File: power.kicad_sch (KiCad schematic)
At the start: 34 parts, among them J11 CON-SOCJ-2155, J12 Header for power lead to QMTE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, J15 Fuse Holder 5A, J33 Header for power lead to QMTE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, J34 Conn_01x04, J35 Conn_01x04, SW2 SW_SPDT_with_shield, U15 LM2678T-5.0

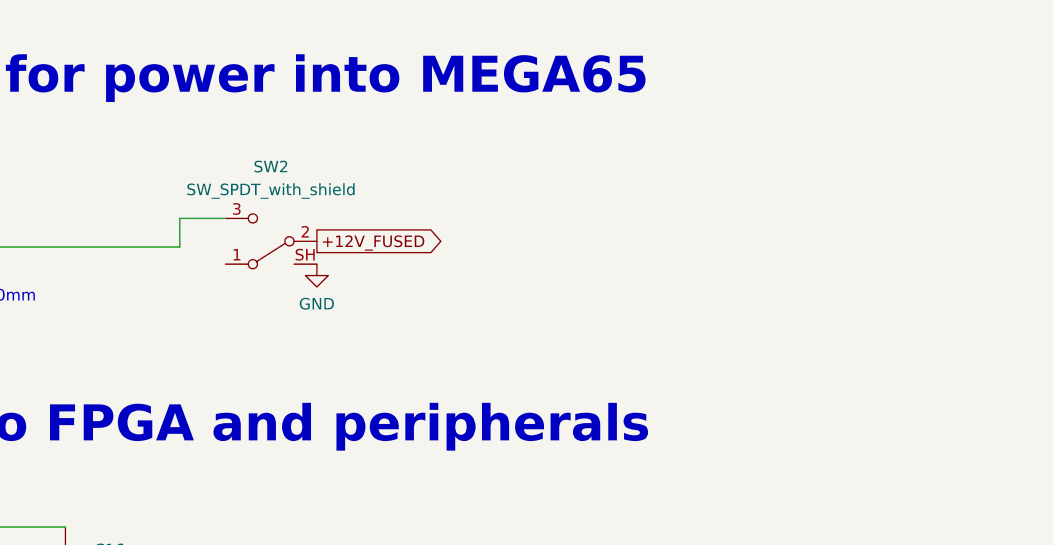
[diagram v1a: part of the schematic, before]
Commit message: add power-bypass, fix DRC violation, U29 is 5V VCC
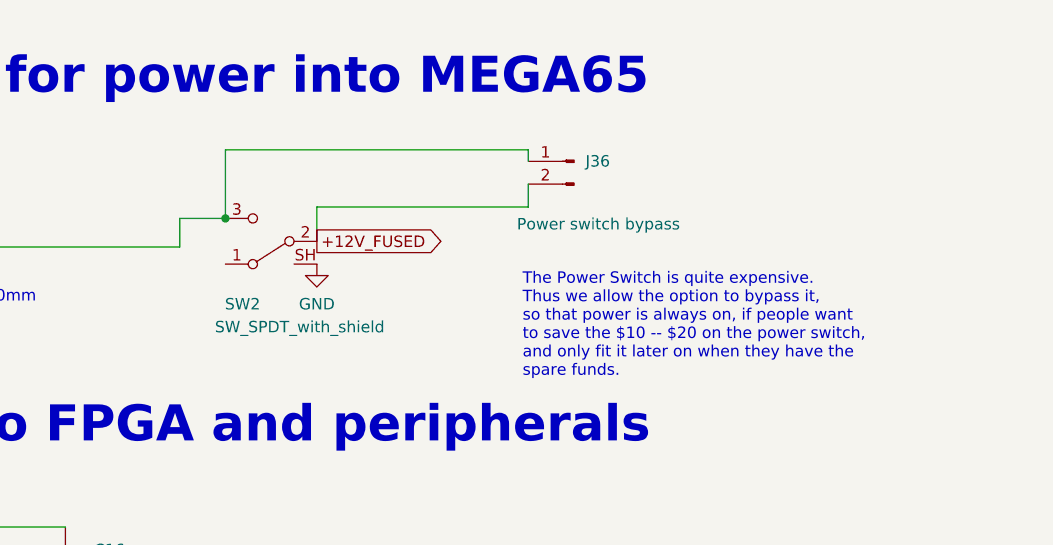
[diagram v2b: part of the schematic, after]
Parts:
- added J36: Power switch bypass, Connector_PinHeader_2.54mm:PinHeader_1x02_P2.54mm_Vertical, symbol Connector:Conn_01x02_Male
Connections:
- net +12V_FUSED: now also J36.2 (Pin_2)
- net at J15.2, SW2.3 (C): now also J36.1 (Pin_1)
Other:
- note added: "The Power Switch is quite expensive. Thus we allow the option to bypass it, so that power is always on, if people want to save the $10 -- $20 on the power switch, and only fit it later on when they have the spare funds."
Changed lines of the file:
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@@
   (junction (at 75.565 85.725) (diameter 0) (color 0 0 0 0)
   )
+  (junction (at 196.215 38.735) (diameter 0) (color 0 0 0 0)
+  )
   (junction (at 265.43 90.17) (diameter 0) (color 0 0 0 0)
   )
@@
     (stroke (width 0) (type default) (color 0 0 0 0))
   )
+  (wire (pts (xy 206.375 37.465) (xy 206.375 41.275))
+    (stroke (width 0) (type default) (color 0 0 0 0))
+  )
   (wire (pts (xy 120.015 98.425) (xy 120.015 107.315))
     (stroke (width 0) (type default) (color 0 0 0 0))
@@
     (stroke (width 0) (type default) (color 0 0 0 0))
   )
+  (wire (pts (xy 229.87 37.465) (xy 229.87 34.925))
+    (stroke (width 0) (type default) (color 0 0 0 0))
+  )
   (wire (pts (xy 112.395 93.345) (xy 112.395 98.425))
     (stroke (width 0) (type default) (color 0 0 0 0))
@@
     (stroke (width 0) (type default) (color 0 0 0 0))
   )
+  (wire (pts (xy 196.215 38.735) (xy 196.215 31.115))
+    (stroke (width 0) (type default) (color 0 0 0 0))
+  )
   (wire (pts (xy 265.43 111.125) (xy 265.43 113.665))
     (stroke (width 0) (type default) (color 0 0 0 0))
   )
+  (wire (pts (xy 206.375 37.465) (xy 229.87 37.465))
+    (stroke (width 0) (type default) (color 0 0 0 0))
+  )
   (wire (pts (xy 257.81 92.71) (xy 265.43 92.71))
     (stroke (width 0) (type default) (color 0 0 0 0))
@@
     (stroke (width 0) (type default) (color 0 0 0 0))
   )
+  (wire (pts (xy 229.87 31.115) (xy 229.87 32.385))
+    (stroke (width 0) (type default) (color 0 0 0 0))
+  )
   (wire (pts (xy 174.625 93.345) (xy 198.755 93.345))
     (stroke (width 0) (type default) (color 0 0 0 0))
@@
   )
   (wire (pts (xy 100.965 85.725) (xy 112.395 85.725))
+    (stroke (width 0) (type default) (color 0 0 0 0))
+  )
+  (wire (pts (xy 196.215 31.115) (xy 229.87 31.115))
     (stroke (width 0) (type default) (color 0 0 0 0))
   )
@@
     (effects (font (size 1.27 1.27)) (justify left bottom))
   )
+  (text "The Power Switch is quite expensive.\nThus we allow the option to bypass it,\nso that power is always on, if people want\nto save the $10 -- $20 on the power switch,\nand only fit it later on when they have the\nspare funds."
+    (at 229.235 56.515 0)
+    (effects (font (size 1.27 1.27)) (justify left bottom))
+  )
   (text "+12V DC 2.1mm Barrell Connector for power into MEGA65"
     (at 63.5 25.4 0)
@@
   )
   (symbol (lib_id "00Project-SDF-60J:SW_SPDT_with_shield") (at 201.295 41.275 180) (unit 1)
-    (in_bom yes) (on_board yes) (fields_autoplaced)
-    (property "Reference" "SW2" (id 0) (at 201.295 33.02 0))
-    (property "Value" "SW_SPDT_with_shield" (id 1) (at 201.295 35.56 0))
+    (in_bom yes) (on_board yes)
+    (property "Reference" "SW2" (id 0) (at 198.12 48.26 0))
+    (property "Value" "SW_SPDT_with_shield" (id 1) (at 204.47 50.8 0))
     (property "Footprint" "snapeda:T103J1AVBE2" (id 2) (at 201.295 41.275 0)
       (effects (font (size 1.27 1.27)) hide)
@@
     (pin "1")
   )
+  (symbol (lib_id "Connector:Conn_01x02_Male") (at 234.95 32.385 0) (mirror y) (unit 1)
+    (in_bom yes) (on_board yes)
+    (property "Reference" "J36" (id 0) (at 236.22 32.3849 0)
+      (effects (font (size 1.27 1.27)) (justify right))
+    )
+    (property "Value" "Power switch bypass" (id 1) (at 228.6 39.37 0)
+      (effects (font (size 1.27 1.27)) (justify right))
+    )
+    (property "Footprint" "Connector_PinHeader_2.54mm:PinHeader_1x02_P2.54mm_Vertical" (id 2) (at 234.95 32.385 0)
+      (effects (font (size 1.27 1.27)) hide)
+    )
+    (property "Datasheet" "~" (id 3) (at 234.95 32.385 0)
+      (effects (font (size 1.27 1.27)) hide)
+    )
+    (pin "1")
+    (pin "2")
+  )
   (symbol (lib_id "Connector:Conn_01x02_Male") (at 146.685 145.415 0) (unit 1)

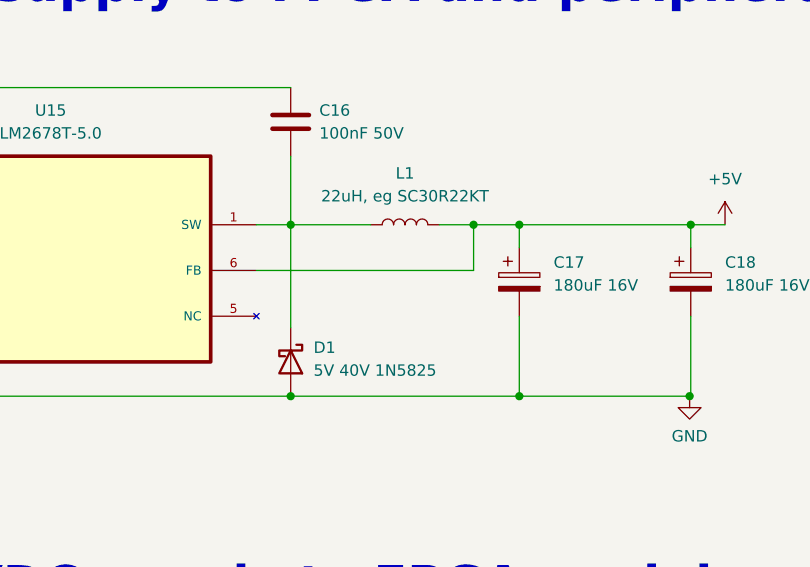
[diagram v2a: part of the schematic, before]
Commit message: update schematic due to BoM requirements
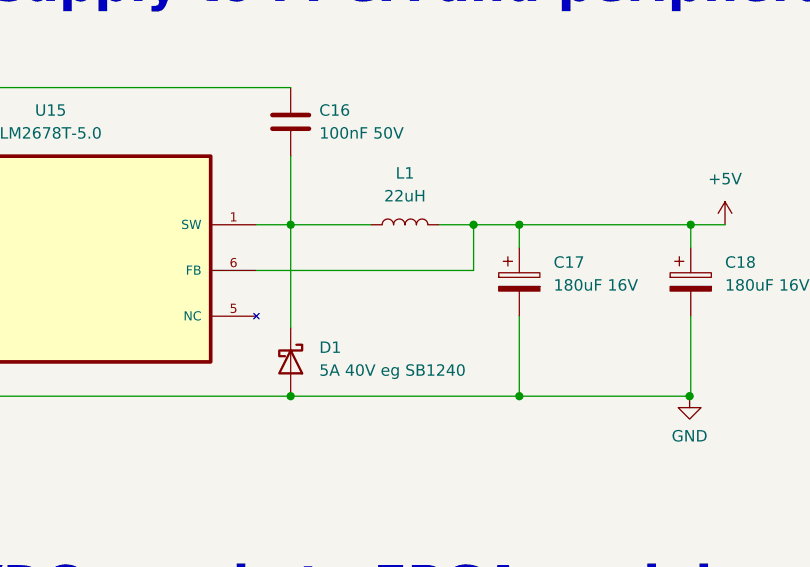
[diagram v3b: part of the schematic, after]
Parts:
- D1: value 5V 40V 1N5825 -> 5A 40V eg SB1240
- L1: value 22uH, eg SC30R22KT -> 22uH
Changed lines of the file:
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@@
     (in_bom yes) (on_board yes) (fields_autoplaced)
     (property "Reference" "L1" (id 0) (at 191.135 82.55 90))
-    (property "Value" "22uH, eg SC30R22KT" (id 1) (at 191.135 85.09 90))
+    (property "Value" "22uH" (id 1) (at 191.135 85.09 90))
     (property "Footprint" "Inductor_THT:L_Axial_L5.0mm_D3.6mm_P10.00mm_Horizontal_Murata_BL01RN1A2A2" (id 2) (at 191.135 88.265 0)
       (effects (font (size 1.27 1.27)) hide)
@@
   (symbol (lib_id "Device:D_Schottky") (at 178.435 103.505 270) (unit 1)
     (in_bom yes) (on_board yes) (fields_autoplaced)
-    (property "Reference" "D1" (id 0) (at 180.975 101.9174 90)
-      (effects (font (size 1.27 1.27)) (justify left))
-    )
-    (property "Value" "5V 40V 1N5825" (id 1) (at 180.975 104.4574 90)
-      (effects (font (size 1.27 1.27)) (justify left))
-    )
+    (property "Reference" "D1" (id 0) (at 181.61 101.9174 90)
+      (effects (font (size 1.27 1.27)) (justify left))
+    )
+    (property "Value" "5A 40V eg SB1240" (id 1) (at 181.61 104.4574 90)
+      (effects (font (size 1.27 1.27)) (justify left))
+    )

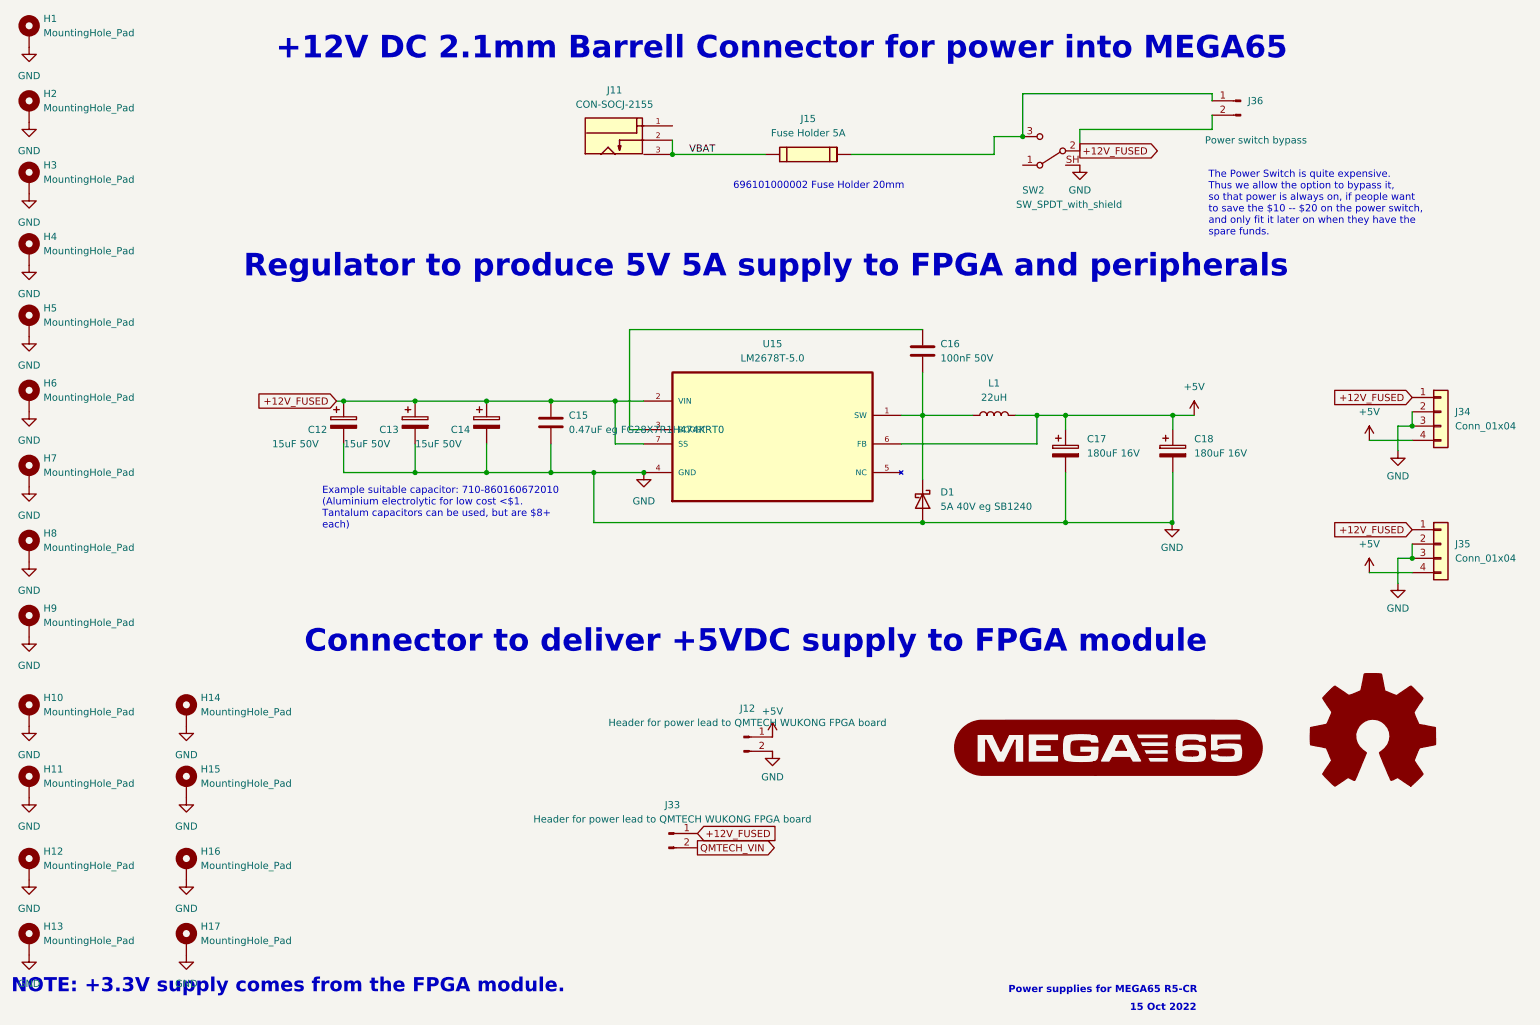
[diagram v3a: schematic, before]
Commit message: rework user port
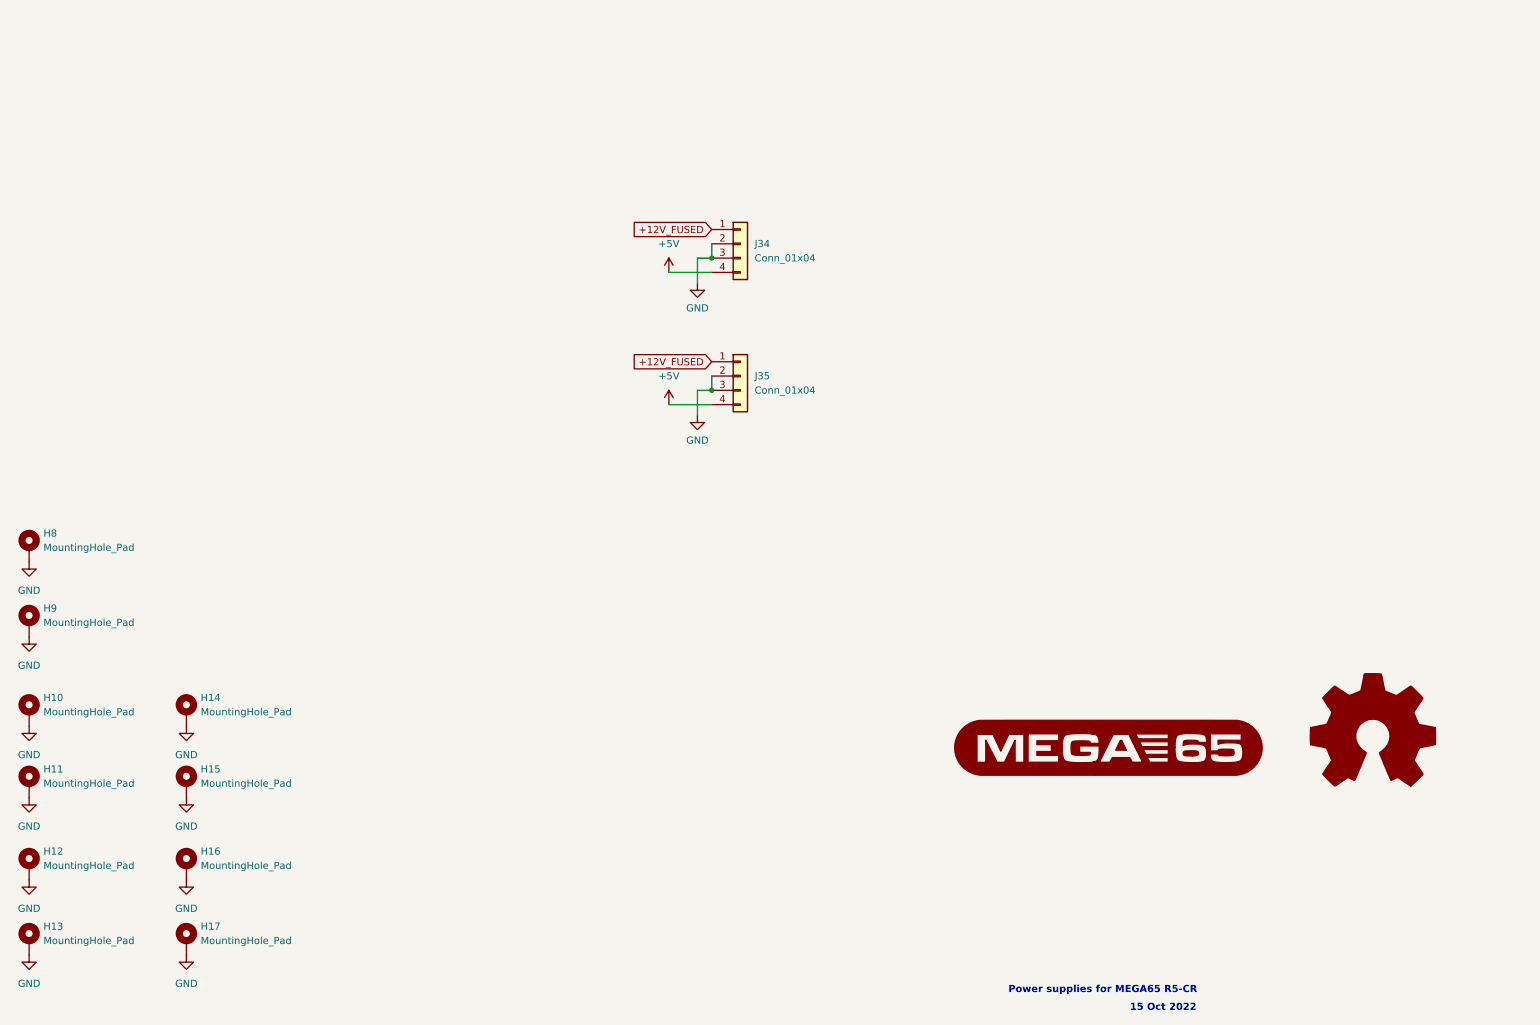
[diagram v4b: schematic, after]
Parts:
- removed C12, C13, C14: 15uF 50V, Capacitor_THT:CP_Radial_D5.0mm_P2.00mm, symbol Device:C_Polarized
- removed C15: 0.47uF eg FG28X7R1H474KRT0, Capacitor_THT:C_Disc_D6.0mm_W4.4mm_P5.00mm, symbol Device:C
- removed C16: 100nF 50V, Capacitor_THT:C_Disc_D6.0mm_W4.4mm_P5.00mm, symbol Device:C
- removed C17, C18: 180uF 16V, Capacitor_THT:CP_Radial_D10.0mm_P5.00mm, symbol Device:C_Polarized
- removed D1: 5A 40V eg SB1240, Diode_THT:D_5KP_P12.70mm_Horizontal, symbol Device:D_Schottky
- removed H1, H2, H3, H4, H5, H6, H7: MountingHole_Pad, MountingHole:MountingHole_3.2mm_M3_DIN965_Pad, symbol Mechanical:MountingHole_Pad
- removed J11: CON-SOCJ-2155, snapeda:GRAVITECH_CON-SOCJ-2155, symbol 00Project-SOCJ-2155:CON-SOCJ-2155
- removed J12, J33: Header for power lead to QMTECH WUKONG FPGA board, Connector_PinHeader_2.54mm:PinHeader_1x02_P2.54mm_Vertical, symbol Connector:Conn_01x02_Male
- removed J15: Fuse Holder 5A, snapeda:696101000002, symbol 00Project-FuseHolder:696101000002
- removed J36: Power switch bypass, Connector_PinHeader_2.54mm:PinHeader_1x02_P2.54mm_Vertical, symbol Connector:Conn_01x02_Male
- removed L1: 22uH, Inductor_THT:L_Axial_L5.0mm_D3.6mm_P10.00mm_Horizontal_Murata_BL01RN1A2A2, symbol Device:L
- removed SW2: SW_SPDT_with_shield, snapeda:T103J1AVBE2, symbol 00Project-SDF-60J:SW_SPDT_with_shield
- removed U15: LM2678T-5.0, snapeda:TO127P457X1016X2052-7P, symbol 00Project-5VReg:LM2678T-5.0
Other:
- note removed: "+12V DC 2.1mm Barrell Connector for power into MEGA65"
- note removed: "696101000002 Fuse Holder 20mm"
- note removed: "Connector to deliver +5VDC supply to FPGA module"
- note removed: "Example suitable capacitor: 710-860160672010 (Aluminium electrolytic for low cost <$1. Tantalum capacitors can be used, but are $8+ each)"
- note removed: "NOTE: +3.3V supply comes from the FPGA module."
- note removed: "Regulator to produce 5V 5A supply to FPGA and peripherals"
- note removed: "The Power Switch is quite expensive. Thus we allow the option to bypass it, so that power is always on, if people want to save the $10 -- $20 on the power switch, and only fit it later on when they have the spare funds."
- moved on the sheet: J34, J35

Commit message: fix remaining problems
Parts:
- added LOGO1: Logo_Open_Hardware_Large, Symbol:OSHW-Logo2_14.6x12mm_SilkScreen, symbol Graphic:Logo_Open_Hardware_Large
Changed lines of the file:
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@@
   (symbol (lib_id "Graphic:Logo_Open_Hardware_Large") (at 258.445 145.415 0) (unit 1)
     (in_bom yes) (on_board yes) (fields_autoplaced)
-    (property "Reference" "#LOGO1" (id 0) (at 258.445 132.715 0)
+    (property "Reference" "LOGO1" (id 0) (at 258.445 132.715 0)
       (effects (font (size 1.27 1.27)) hide)
     )
@@
       (effects (font (size 1.27 1.27)) hide)
     )
-    (property "Footprint" "Symbol:OSHW-Logo2_14.6x12mm_SilkScreen" (id 2) (at 258.445 145.415 0)
-      (effects (font (size 1.27 1.27)) hide)
-    )
+    (property "Footprint" "Symbol:OSHW-Logo2_14.6x12mm_SilkScreen" (id 2) (at 258.445 132.08 0))
     (property "Datasheet" "~" (id 3) (at 258.445 145.415 0)
       (effects (font (size 1.27 1.27)) hide)

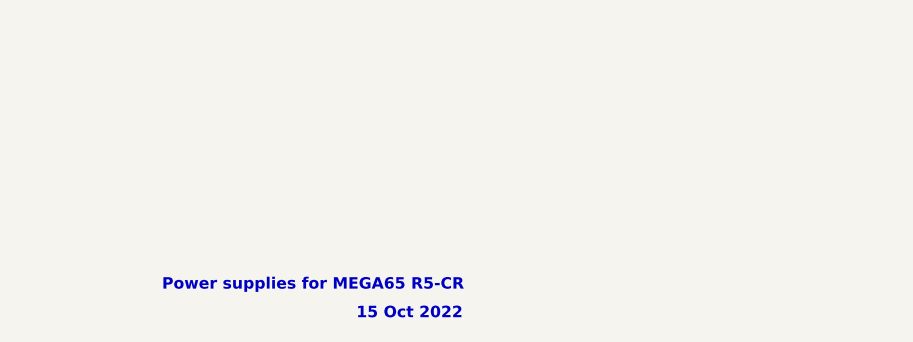
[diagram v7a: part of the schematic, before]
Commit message: correct stale board ID
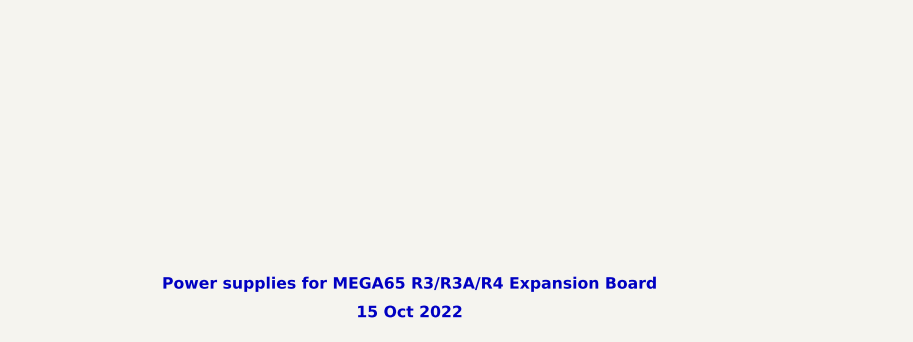
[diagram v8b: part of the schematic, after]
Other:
- note added: "Power supplies for MEGA65 R3/R3A/R4 Expansion Board"
- note removed: "Power supplies for MEGA65 R5-CR"
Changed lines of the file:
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@@
     )
   )
-  (text "Power supplies for MEGA65 R5-CR" (at 193.675 191.135 0)
+  (text "Power supplies for MEGA65 R3/R3A/R4 Expansion Board" (at 193.675 191.135 0)
     (effects (font (size 1.27 1.27) bold) (justify left bottom))
   )
